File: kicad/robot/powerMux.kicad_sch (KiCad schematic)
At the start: 8 parts, among them Q1 Q_NMOS_GDS, U4 NCP3901

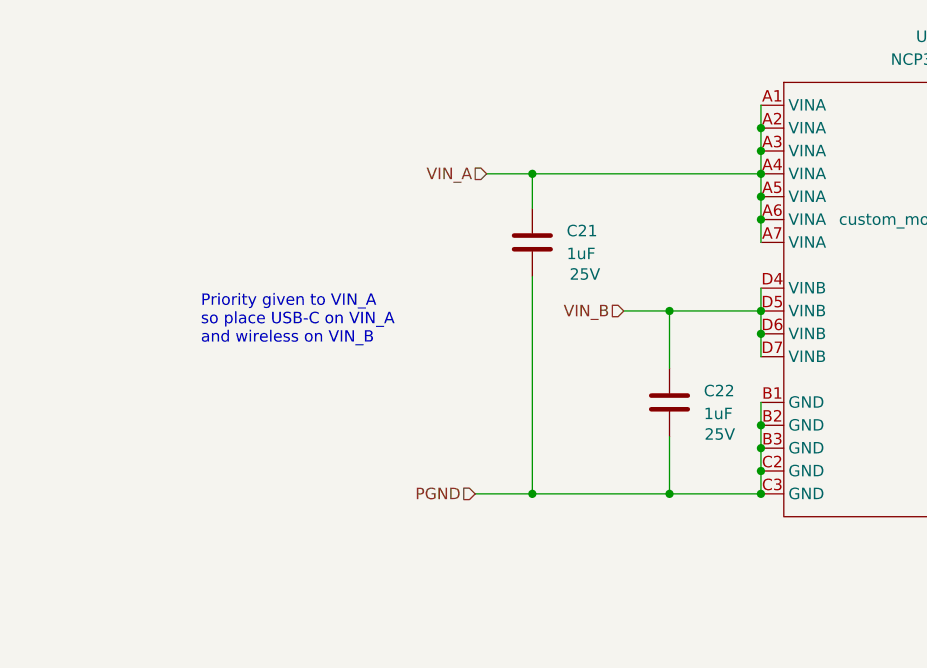
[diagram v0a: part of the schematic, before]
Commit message: Add current breaks between each section of hardware.
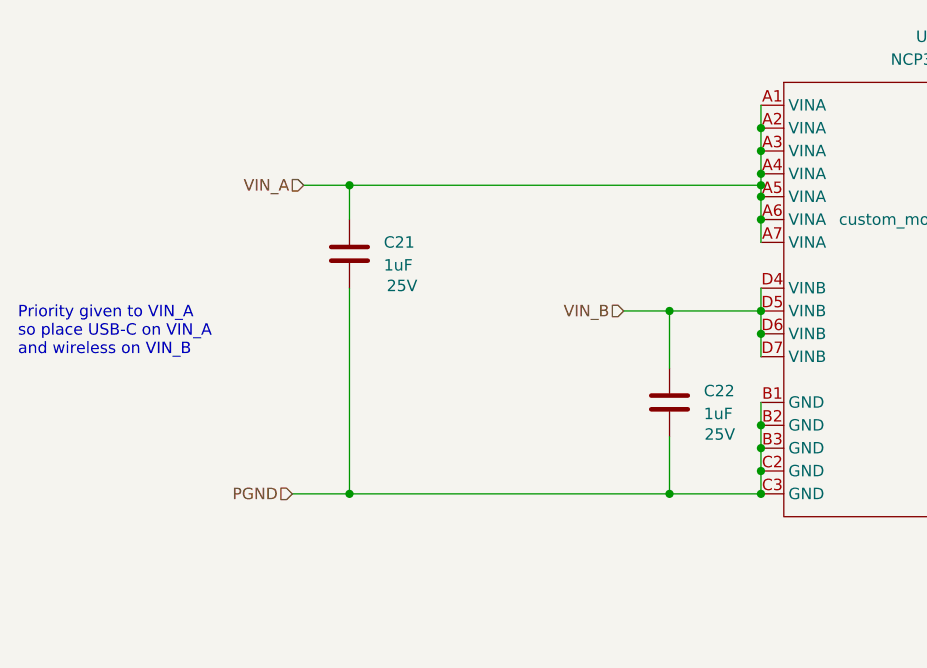
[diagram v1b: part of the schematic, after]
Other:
- moved on the sheet: C21
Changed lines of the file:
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@@
   (junction (at 121.92 83.82) (diameter 0) (color 0 0 0 0)
   )
+  (junction (at 121.92 90.17) (diameter 0) (color 0 0 0 0)
+  )
   (junction (at 121.92 121.92) (diameter 0) (color 0 0 0 0)
   )
@@
   (junction (at 160.02 86.36) (diameter 0) (color 0 0 0 0)
   )
-  (junction (at 96.52 88.9) (diameter 0) (color 0 0 0 0)
+  (junction (at 76.2 90.17) (diameter 0) (color 0 0 0 0)
   )
   (junction (at 160.02 91.44) (diameter 0) (color 0 0 0 0)
@@
   (junction (at 121.92 104.14) (diameter 0) (color 0 0 0 0)
   )
-  (junction (at 96.52 124.46) (diameter 0) (color 0 0 0 0)
+  (junction (at 76.2 124.46) (diameter 0) (color 0 0 0 0)
   )
   (junction (at 121.92 91.44) (diameter 0) (color 0 0 0 0)
   )
-  (wire (pts (xy 91.44 88.9) (xy 96.52 88.9))
+  (wire (pts (xy 71.12 90.17) (xy 76.2 90.17))
     (stroke (width 0) (type default))
   )
@@
     (stroke (width 0) (type default))
   )
-  (wire (pts (xy 96.52 88.9) (xy 121.92 88.9))
+  (wire (pts (xy 76.2 90.17) (xy 121.92 90.17))
     (stroke (width 0) (type default))
   )
@@
     (stroke (width 0) (type default))
   )
-  (wire (pts (xy 96.52 88.9) (xy 96.52 92.71))
+  (wire (pts (xy 76.2 90.17) (xy 76.2 93.98))
     (stroke (width 0) (type default))
   )
@@
     (stroke (width 0) (type default))
   )
-  (wire (pts (xy 90.17 124.46) (xy 96.52 124.46))
+  (wire (pts (xy 69.85 124.46) (xy 76.2 124.46))
     (stroke (width 0) (type default))
   )
@@
     (stroke (width 0) (type default))
   )
-  (wire (pts (xy 96.52 100.33) (xy 96.52 124.46))
+  (wire (pts (xy 76.2 101.6) (xy 76.2 124.46))
     (stroke (width 0) (type default))
   )
@@
     (stroke (width 0) (type default))
   )
+  (wire (pts (xy 121.92 90.17) (xy 121.92 91.44))
+    (stroke (width 0) (type default))
+  )
   (wire (pts (xy 173.99 127) (xy 173.99 129.54))
     (stroke (width 0) (type default))
   )
-  (wire (pts (xy 96.52 124.46) (xy 111.76 124.46))
+  (wire (pts (xy 76.2 124.46) (xy 111.76 124.46))
     (stroke (width 0) (type default))
   )
@@
     (stroke (width 0) (type default))
   )
-  (wire (pts (xy 121.92 88.9) (xy 121.92 91.44))
-    (stroke (width 0) (type default))
-  )
   (wire (pts (xy 196.85 81.28) (xy 201.93 81.28))
     (stroke (width 0) (type default))
@@
   )
   (wire (pts (xy 106.68 104.14) (xy 111.76 104.14))
+    (stroke (width 0) (type default))
+  )
+  (wire (pts (xy 121.92 90.17) (xy 121.92 88.9))
     (stroke (width 0) (type default))
   )
@@
   )
   (text "Priority given to VIN_A\nso place USB-C on VIN_A\nand wireless on VIN_B"
-    (at 59.69 107.95 0)
+    (at 39.37 109.22 0)
     (effects (font (size 1.27 1.27)) (justify left bottom))
   )
@@
     (effects (font (size 1.27 1.27)) (justify left bottom))
   )
-  (hierarchical_label "PGND" (shape input) (at 90.17 124.46 180) (fields_autoplaced)
+  (hierarchical_label "PGND" (shape input) (at 69.85 124.46 180) (fields_autoplaced)
     (effects (font (size 1.27 1.27)) (justify right))
   )
@@
     (effects (font (size 1.27 1.27)) (justify right))
   )
-  (hierarchical_label "VIN_A" (shape input) (at 91.44 88.9 180) (fields_autoplaced)
+  (hierarchical_label "VIN_A" (shape input) (at 71.12 90.17 180) (fields_autoplaced)
     (effects (font (size 1.27 1.27)) (justify right))
   )
@@
     )
   )
-  (symbol (lib_id "Device:C") (at 96.52 96.52 0) (unit 1)
+  (symbol (lib_id "Device:C") (at 76.2 97.79 0) (unit 1)
     (in_bom yes) (on_board yes) (dnp no)
-    (property "Reference" "C21" (at 100.33 95.2499 0)
-      (effects (font (size 1.27 1.27)) (justify left))
-    )
-    (property "Value" "1uF" (at 100.33 97.7899 0)
-      (effects (font (size 1.27 1.27)) (justify left))
-    )
-    (property "Footprint" "Capacitor_SMD:C_0402_1005Metric" (at 97.4852 100.33 0)
-      (effects (font (size 1.27 1.27)) hide)
-    )
-    (property "Datasheet" "~" (at 96.52 96.52 0)
-      (effects (font (size 1.27 1.27)) hide)
-    )
-    (property "Description" "25V" (at 102.362 100.076 0)
+    (property "Reference" "C21" (at 80.01 96.5199 0)
+      (effects (font (size 1.27 1.27)) (justify left))
+    )
+    (property "Value" "1uF" (at 80.01 99.0599 0)
+      (effects (font (size 1.27 1.27)) (justify left))
+    )
+    (property "Footprint" "Capacitor_SMD:C_0402_1005Metric" (at 77.1652 101.6 0)
+      (effects (font (size 1.27 1.27)) hide)
+    )
+    (property "Datasheet" "~" (at 76.2 97.79 0)
+      (effects (font (size 1.27 1.27)) hide)
+    )
+    (property "Description" "25V" (at 82.042 101.346 0)
       (effects (font (size 1.27 1.27)))
     )
-    (property "Manufacturer" "Murata" (at 96.52 96.52 0)
-      (effects (font (size 1.27 1.27)) hide)
-    )
-    (property "Part Number" "GRM155R61E105KA12D" (at 96.52 96.52 0)
-      (effects (font (size 1.27 1.27)) hide)
-    )
+    (property "Manufacturer" "Murata" (at 76.2 97.79 0)
+      (effects (font (size 1.27 1.27)) hide)
+    )
+    (property "Part Number" "GRM155R61E105KA12D" (at 76.2 97.79 0)
+      (effects (font (size 1.27 1.27)) hide)
+    )

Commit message: Updated voltage translation mosfets to lower V_th mosfets
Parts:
- Q1: Manufacturer Toshiba -> ANBON SEMICONDUCTOR (INT'L) LIMITED; Part Number T2N7002AK,LM -> BSS138
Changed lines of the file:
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@@
       (effects (font (size 1.27 1.27)) hide)
     )
-    (property "Part Number" "T2N7002AK,LM" (at 207.01 81.28 0)
+    (property "Part Number" "BSS138" (at 207.01 81.28 0)
       (effects (font (size 1.27 1.27)) hide)
     )
-    (property "Manufacturer" "Toshiba" (at 207.01 81.28 0)
+    (property "Manufacturer" "ANBON SEMICONDUCTOR (INT'L) LIMITED" (at 207.01 81.28 0)
       (effects (font (size 1.27 1.27)) hide)
     )
+    (property "Manufacturer Part Number" "" (at 207.01 81.28 0)
+      (effects (font (size 1.27 1.27)) hide)
+    )
+    (property "Supplier" "" (at 207.01 81.28 0)
+      (effects (font (size 1.27 1.27)) hide)
+    )
+    (property "Supplier Part Number" "" (at 207.01 81.28 0)
+      (effects (font (size 1.27 1.27)) hide)
+    )
+    (property "Populated" "" (at 207.01 81.28 0)
+      (effects (font (size 1.27 1.27)) hide)
+    )
+    (property "ID" "" (at 207.01 81.28 0)
+      (effects (font (size 1.27 1.27)) hide)
+    )

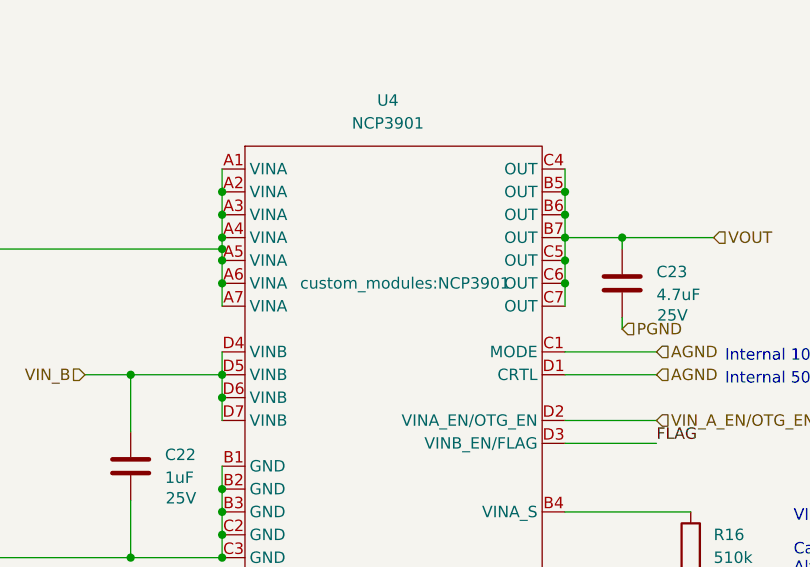
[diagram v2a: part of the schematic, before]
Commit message: updated all footprint fields in schematic symbols with local robot ones
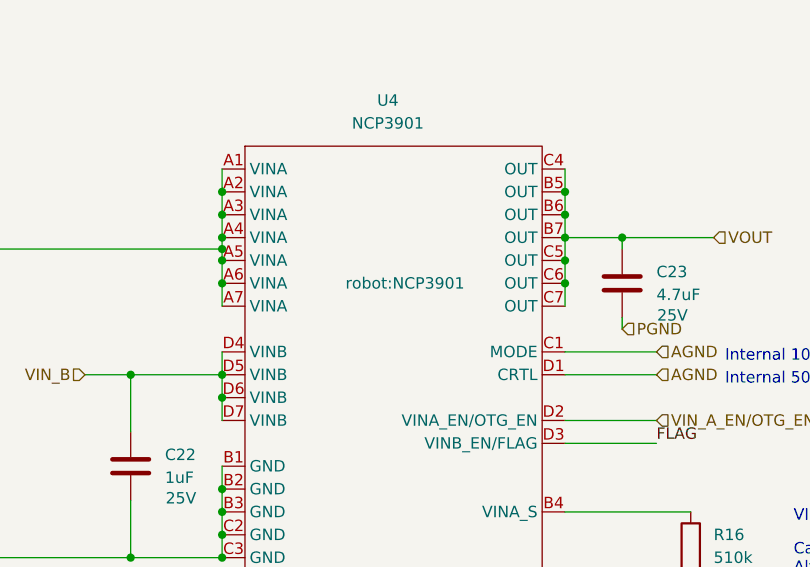
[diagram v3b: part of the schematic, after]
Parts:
- C21, C22: footprint Capacitor_SMD:C_0402_1005Metric -> robot:C_0402_1005Metric
- C23: footprint Capacitor_SMD:C_0805_2012Metric -> robot:C_0805_2012Metric
- Q1: footprint Package_TO_SOT_SMD:SOT-23 -> robot:SOT-23
- R16, R17, R18: footprint Resistor_SMD:R_0603_1608Metric -> robot:R_0603_1608Metric
- U4: footprint custom_modules:NCP3901 -> robot:NCP3901
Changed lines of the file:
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@@
       (effects (font (size 1.27 1.27)) (justify left))
     )
-    (property "Footprint" "Resistor_SMD:R_0603_1608Metric" (at 172.212 123.19 90)
+    (property "Footprint" "robot:R_0603_1608Metric" (at 172.212 123.19 90)
       (effects (font (size 1.27 1.27)) hide)
     )
@@
       (effects (font (size 1.27 1.27)) (justify left))
     )
-    (property "Footprint" "Capacitor_SMD:C_0805_2012Metric" (at 167.3352 97.79 0)
+    (property "Footprint" "robot:C_0805_2012Metric" (at 167.3352 97.79 0)
       (effects (font (size 1.27 1.27)) hide)
     )
@@
       (effects (font (size 1.27 1.27)) (justify left))
     )
-    (property "Footprint" "Package_TO_SOT_SMD:SOT-23" (at 212.09 78.74 0)
+    (property "Footprint" "robot:SOT-23" (at 212.09 78.74 0)
       (effects (font (size 1.27 1.27)) hide)
     )
@@
       (effects (font (size 1.27 1.27)) (justify left))
     )
-    (property "Footprint" "Capacitor_SMD:C_0402_1005Metric" (at 112.7252 118.11 0)
+    (property "Footprint" "robot:C_0402_1005Metric" (at 112.7252 118.11 0)
       (effects (font (size 1.27 1.27)) hide)
     )
@@
       (effects (font (size 1.27 1.27)) (justify left))
     )
-    (property "Footprint" "Resistor_SMD:R_0603_1608Metric" (at 207.772 67.31 90)
+    (property "Footprint" "robot:R_0603_1608Metric" (at 207.772 67.31 90)
       (effects (font (size 1.27 1.27)) hide)
     )
@@
       (effects (font (size 1.27 1.27)) (justify left))
     )
-    (property "Footprint" "Capacitor_SMD:C_0402_1005Metric" (at 77.1652 101.6 0)
+    (property "Footprint" "robot:C_0402_1005Metric" (at 77.1652 101.6 0)
       (effects (font (size 1.27 1.27)) hide)
     )
@@
       (effects (font (size 1.27 1.27)))
     )
-    (property "Footprint" "custom_modules:NCP3901" (at 142.24 93.98 0)
+    (property "Footprint" "robot:NCP3901" (at 142.24 93.98 0)
       (effects (font (size 1.27 1.27)))
     )
@@
       (effects (font (size 1.27 1.27)) (justify left))
     )
-    (property "Footprint" "Resistor_SMD:R_0603_1608Metric" (at 172.212 135.89 90)
-      (effects (font (size 1.27 1.27)) hide)
-    )
+    (property "Footprint" "robot:R_0603_1608Metric" (at 172.212 135.89 90)
+      (effects (font (size 1.27 1.27)) hide)
+    )

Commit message: Exported all schematic symbols to local robot and refer to them in all symbols
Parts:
- C21, C22, C23: symbol Device:C -> robot:C
- Q1: symbol Device:Q_NMOS_GSD -> robot:Q_NMOS_GSD
- R16, R17, R18: symbol Device:R -> robot:R
- U4: symbol custom_modules:NCP3901 -> robot:NCP3901
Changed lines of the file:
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@@
     (effects (font (size 1.27 1.27)) (justify left))
   )
-  (symbol (lib_id "Device:R") (at 173.99 123.19 0) (unit 1)
+  (symbol (lib_id "robot:R") (at 173.99 123.19 0) (unit 1)
     (in_bom yes) (on_board yes) (dnp no) (fields_autoplaced)
     (property "Reference" "R16" (at 176.53 121.9199 0)
@@
     )
   )
-  (symbol (lib_id "Device:C") (at 166.37 93.98 0) (unit 1)
+  (symbol (lib_id "robot:C") (at 166.37 93.98 0) (unit 1)
     (in_bom yes) (on_board yes) (dnp no)
     (property "Reference" "C23" (at 170.18 92.7099 0)
@@
     )
   )
-  (symbol (lib_id "Device:Q_NMOS_GSD") (at 207.01 81.28 0) (unit 1)
+  (symbol (lib_id "robot:Q_NMOS_GSD") (at 207.01 81.28 0) (unit 1)
     (in_bom yes) (on_board yes) (dnp no) (fields_autoplaced)
     (property "Reference" "Q1" (at 213.36 80.0099 0)
@@
     )
   )
-  (symbol (lib_id "Device:C") (at 111.76 114.3 0) (unit 1)
+  (symbol (lib_id "robot:C") (at 111.76 114.3 0) (unit 1)
     (in_bom yes) (on_board yes) (dnp no)
     (property "Reference" "C22" (at 115.57 113.0299 0)
@@
     )
   )
-  (symbol (lib_id "Device:R") (at 209.55 67.31 0) (unit 1)
+  (symbol (lib_id "robot:R") (at 209.55 67.31 0) (unit 1)
     (in_bom yes) (on_board yes) (dnp no) (fields_autoplaced)
     (property "Reference" "R18" (at 212.09 66.0399 0)
@@
     )
   )
-  (symbol (lib_id "Device:C") (at 76.2 97.79 0) (unit 1)
+  (symbol (lib_id "robot:C") (at 76.2 97.79 0) (unit 1)
     (in_bom yes) (on_board yes) (dnp no)
     (property "Reference" "C21" (at 80.01 96.5199 0)
@@
     )
   )
-  (symbol (lib_id "custom_modules:NCP3901") (at 142.24 101.6 0) (unit 1)
+  (symbol (lib_id "robot:NCP3901") (at 142.24 101.6 0) (unit 1)
     (in_bom yes) (on_board yes) (dnp no) (fields_autoplaced)
     (property "Reference" "U4" (at 140.335 73.66 0)
@@
     )
   )
-  (symbol (lib_id "Device:R") (at 173.99 135.89 0) (unit 1)
+  (symbol (lib_id "robot:R") (at 173.99 135.89 0) (unit 1)
     (in_bom yes) (on_board yes) (dnp no) (fields_autoplaced)
     (property "Reference" "R17" (at 176.53 134.6199 0)

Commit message: Removing a bunch of unneccesary symbol properties
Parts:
- U4: Stock 25 -> (none)
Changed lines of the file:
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@@
-      (effects (font (size 1.27 1.27)) hide)
-    )
-    (property "Manufacturer Part Number" "" (at 207.01 81.28 0)
-      (effects (font (size 1.27 1.27)) hide)
-    )
-    (property "Supplier" "" (at 207.01 81.28 0)
-      (effects (font (size 1.27 1.27)) hide)
-    )
-    (property "Supplier Part Number" "" (at 207.01 81.28 0)
-      (effects (font (size 1.27 1.27)) hide)
-    )
-    (property "Populated" "" (at 207.01 81.28 0)
-      (effects (font (size 1.27 1.27)) hide)
-    )
-    (property "ID" "" (at 207.01 81.28 0)
       (effects (font (size 1.27 1.27)) hide)
     )
@@
       (effects (font (size 1.27 1.27)) hide)
     )
-    (property "Stock" "25" (at 142.24 101.6 0)
-      (effects (font (size 1.27 1.27)) hide)
-    )

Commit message: Updating symbol fields for BOM completion.
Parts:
- R17: Part Number RMCF0603JG100K -> RMCF0603FT100K
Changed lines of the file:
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@@
       (effects (font (size 1.27 1.27)) hide)
     )
-    (property "Part Number" "RMCF0603JG100K" (at 173.99 135.89 0)
+    (property "Part Number" "RMCF0603FT100K" (at 173.99 135.89 0)
       (effects (font (size 1.27 1.27)) hide)
     )

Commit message: fixing a few more BOM related issues
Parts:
- R17: Manufacturer Stackpole Electronics -> Walsin Technology; Part Number RMCF0603FT100K -> WR06X1003FTL; Stock (none) -> 100
- U4: Stock (none) -> 19
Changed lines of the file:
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@@
+      (effects (font (size 1.27 1.27)) hide)
+    )
+    (property "Stock" "" (at 173.99 123.19 0)
       (effects (font (size 1.27 1.27)) hide)
     )
@@
       (effects (font (size 1.27 1.27)) hide)
     )
+    (property "Stock" "" (at 166.37 93.98 0)
+      (effects (font (size 1.27 1.27)) hide)
+    )
     (pin "1")
     (pin "2")
@@
     )
     (property "Manufacturer" "ANBON SEMICONDUCTOR (INT'L) LIMITED" (at 207.01 81.28 0)
+      (effects (font (size 1.27 1.27)) hide)
+    )
+    (property "Stock" "" (at 207.01 81.28 0)
       (effects (font (size 1.27 1.27)) hide)
     )
@@
       (effects (font (size 1.27 1.27)) hide)
     )
+    (property "Stock" "" (at 111.76 114.3 0)
+      (effects (font (size 1.27 1.27)) hide)
+    )
     (pin "1")
     (pin "2")
@@
     )
     (property "Part Number" "RMCF0603JT47K0" (at 209.55 67.31 0)
+      (effects (font (size 1.27 1.27)) hide)
+    )
+    (property "Stock" "" (at 209.55 67.31 0)
       (effects (font (size 1.27 1.27)) hide)
     )
@@
       (effects (font (size 1.27 1.27)) hide)
     )
+    (property "Stock" "" (at 76.2 97.79 0)
+      (effects (font (size 1.27 1.27)) hide)
+    )
     (pin "1")
     (pin "2")
@@
     )
     (property "Manufacturer" "onsemi" (at 142.24 101.6 0)
+      (effects (font (size 1.27 1.27)) hide)
+    )
+    (property "Stock" "19" (at 142.24 101.6 0)
       (effects (font (size 1.27 1.27)) hide)
     )
@@
       (effects (font (size 1.27 1.27)) hide)
     )
-    (property "Manufacturer" "Stackpole Electronics" (at 173.99 135.89 0)
-      (effects (font (size 1.27 1.27)) hide)
-    )
-    (property "Part Number" "RMCF0603FT100K" (at 173.99 135.89 0)
-      (effects (font (size 1.27 1.27)) hide)
-    )
+    (property "Manufacturer" "Walsin Technology" (at 173.99 135.89 0)
+      (effects (font (size 1.27 1.27)) hide)
+    )
+    (property "Part Number" "WR06X1003FTL" (at 173.99 135.89 0)
+      (effects (font (size 1.27 1.27)) hide)
+    )
+    (property "Stock" "100" (at 173.99 135.89 0)
+      (effects (font (size 1.27 1.27)) hide)
+    )
